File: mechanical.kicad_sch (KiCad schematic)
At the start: 0 parts

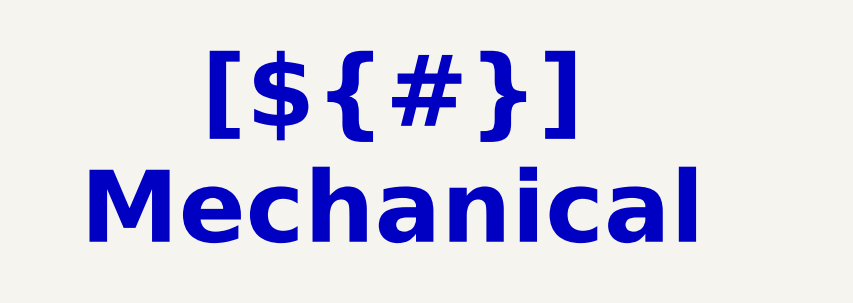
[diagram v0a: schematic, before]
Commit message: SCH[Sens & Inputs, Logic]: Started on sens and inputs condtiong, Logic page drawn. Need to add notes still.
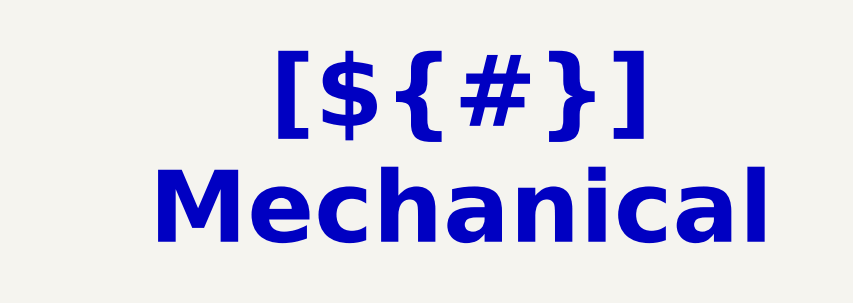
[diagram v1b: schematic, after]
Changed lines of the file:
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@@
 	(text_box "[${#}] ${TITLE}"
 		(exclude_from_sim no)
-		(at 93.98 15.24 0)
+		(at 101.6 15.24 0)
 		(size 96.52 12.7)
 		(margins 5.9999 5.9999 5.9999 5.9999)

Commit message: PCB[Layout, Mounting]:Inital layout and edgecut/hole placment.
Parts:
- added FID1, FID2, FID3: Fiducial, Fiducial:Fiducial_0.5mm_Mask1mm, symbol Mechanical:Fiducial
- added G1: SAE Electric logo, remote_sae_electric_logo:SAE_Electric_Logo_10mm, symbol remote_sae_electric_logo:LOGO
- added G2: BMD Logo, remote_bmd_logo:BDM_Logo_100mm, symbol remote_bmd_logo:BMD LOGO
- added H1, H2, H3, H4, H5: MountingHole, MountingHole:MountingHole_3.2mm_M3, symbol Mechanical:MountingHole
